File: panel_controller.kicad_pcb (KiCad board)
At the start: 2 copper layers, 105.5 x 88.5 mm, 17 parts, among them J1 Screw_Terminal_01x04, J2 SSW-104-01-F-S, J3 Screw_Terminal_01x03, J4 Screw_Terminal_01x02, J5 SSW-108-02-G-D, U1 ESP32-DEVKIT-V1

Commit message: pcb clock v1.5
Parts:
- moved H3 136.8 mm to (82.5, 125.0), turned to 180 degrees
- moved J5 105.8 mm to (121.4, 117.5), turned to -90 degrees
- moved H4 101.5 mm to (82.1, 48.0), turned to 0 degrees
- moved J4 94.9 mm to (95.5, 114.0), turned to -90 degrees
- moved J1 80.3 mm to (95.5, 53.5), turned to -90 degrees
- moved J3 77.7 mm to (95.5, 86.5), turned to -90 degrees
- moved H1 72.2 mm to (196.4, 47.9), turned to 0 degrees
- moved R7 71.5 mm to (109.4, 74.1), turned to 0 degrees
- moved R6 70.0 mm to (109.3, 67.5), turned to 0 degrees
- moved R5 69.6 mm to (109.3, 60.9), turned to 0 degrees
- moved H2 64.7 mm to (196.3, 124.8), turned to 180 degrees
- moved R1 55.4 mm to (124.5, 56.5), turned to 0 degrees
- moved R2 50.2 mm to (124.5, 63.1), turned to 0 degrees
- moved R3 46.2 mm to (124.5, 69.7), turned to 0 degrees
- moved R4 43.9 mm to (124.5, 76.2), turned to 0 degrees
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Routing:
- net Net-(U1-D23): track 141.6 -> 75.7 mm, vias 1 -> 0
- net +5V: track 55.8 -> 111.8 mm
- net Net-(U1-D15): track 103.8 -> 52.3 mm, vias 1 -> 2
- net Net-(U1-D4): track 99.7 -> 48.4 mm
- net Net-(U1-D19): track 121.0 -> 70.0 mm, vias 1 -> 2
- net Net-(U1-D2): track 97.2 -> 48.7 mm
- net Net-(U1-D5): track 105.8 -> 58.9 mm
- net Net-(U1-D18): track 116.1 -> 69.3 mm, vias 2 -> 1
- net Net-(U1-D32): track 30.7 -> 62.9 mm
- net Net-(U1-D33): track 28.7 -> 60.8 mm, vias 1 -> 0
- net Net-(J3-Pin_2): track 63.2 -> 95.0 mm, vias 0 -> 1
- net +3V3: track 116.3 -> 148.1 mm, vias 2 -> 1
- net Net-(U1-D22): track 58.1 -> 35.2 mm
- net Net-(J1-Pin_3): track 38.8 -> 18.3 mm
- net Net-(U1-D21): track 54.7 -> 34.3 mm
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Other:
- board size 105.5 x 88.5 mm -> 127.2 x 90 mm

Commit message: pcb clock v1.6
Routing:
- net Net-(U1-D14): track 87.1 -> 113.0 mm
- net +3V3: track 148.1 -> 167.4 mm, vias 1 -> 2
- net GND: track 200.6 -> 215.5 mm
- net Net-(U1-D26): track 92.2 -> 106.5 mm, vias 2 -> 0
- net +5V: track 111.8 -> 122.3 mm
- net Net-(U1-D18): track 69.3 -> 60.0 mm
- net Net-(U1-D25): track 78.0 -> 87.2 mm, vias 1 -> 2
- net Net-(J3-Pin_2): track 95.0 -> 102.1 mm, vias 1 -> 3
- net Net-(U1-D12): track 100.3 -> 95.7 mm, vias 2 -> 0
- net Net-(U1-D13): track 77.4 -> 81.5 mm, vias 1 -> 2
- net Net-(U1-D4): track 48.4 -> 52.5 mm
- net Net-(U1-D33): track 60.8 -> 57.7 mm
- net Net-(U1-D5): track 58.9 -> 55.9 mm
- net Net-(U1-D21): track 34.3 -> 37.2 mm, vias 0 -> 1
- net Net-(U1-D2): track 48.7 -> 46.1 mm
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
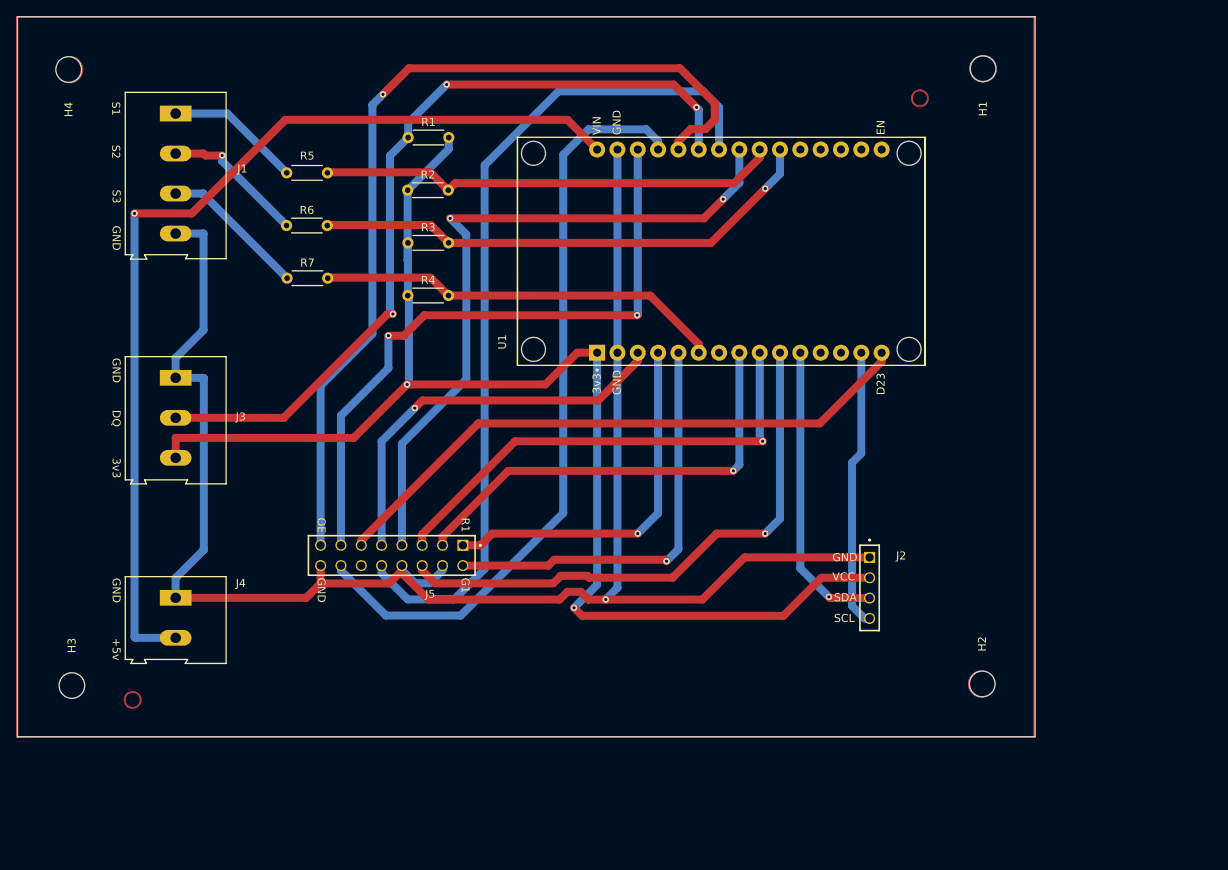
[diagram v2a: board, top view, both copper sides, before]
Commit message: pcb clock v1.7 rerouting for proper track width
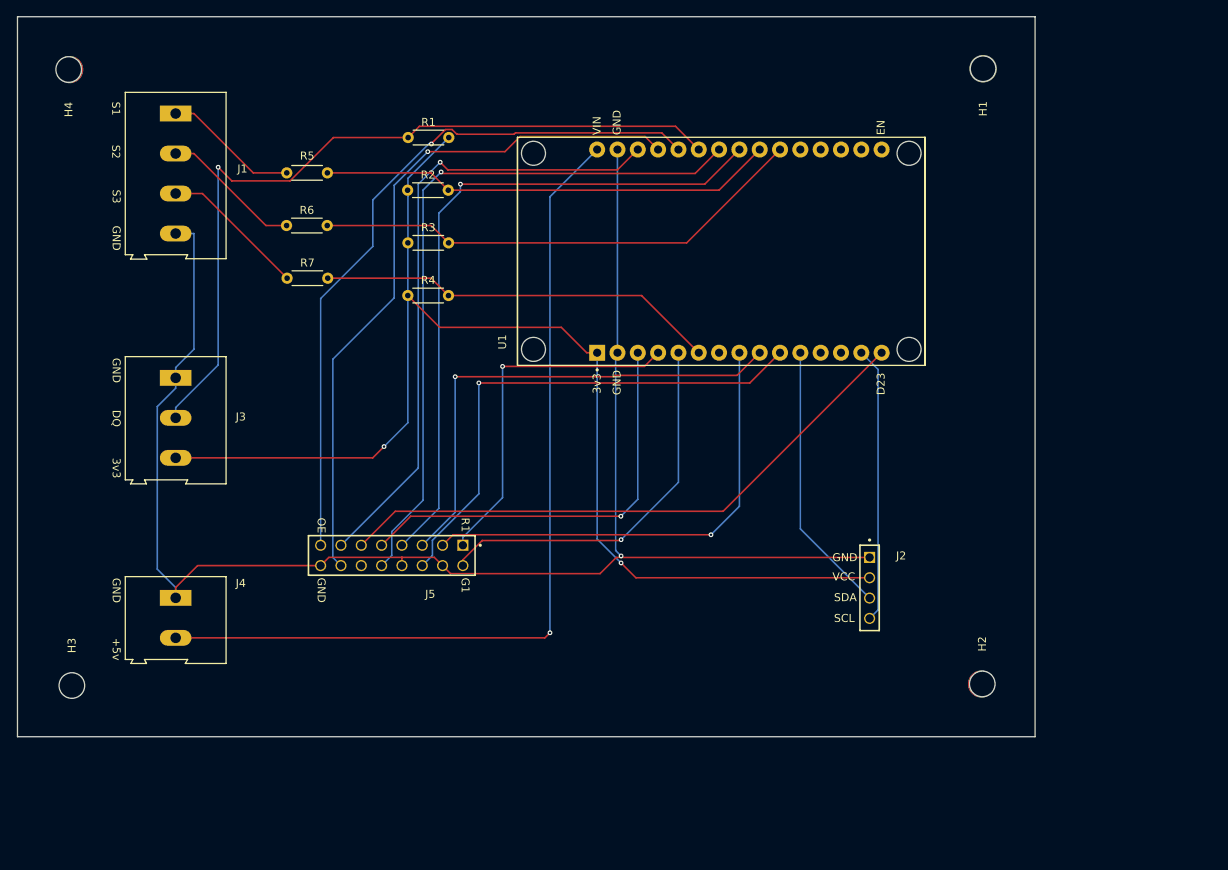
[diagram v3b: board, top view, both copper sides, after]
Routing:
- net Net-(U1-D14): track 113.0 -> 88.9 mm
- net GND: track 215.5 -> 194.3 mm
- net Net-(U1-D26): track 106.5 -> 88.3 mm, vias 0 -> 1
- net +5V: track 122.3 -> 109.9 mm
- net +3V3: track 167.4 -> 155.4 mm
- net Net-(U1-D12): track 95.7 -> 87.3 mm, vias 0 -> 1
- net Net-(U1-D19): track 70.3 -> 65.0 mm
- net Net-(U1-D4): track 52.5 -> 48.0 mm
- net Net-(J3-Pin_2): track 102.1 -> 98.3 mm, vias 3 -> 1
- net Net-(U1-D21): track 37.2 -> 34.3 mm, vias 1 -> 0
- net Net-(U1-D15): track 50.2 -> 52.7 mm
- net Net-(U1-D5): track 55.9 -> 58.3 mm
- net Net-(U1-D13): track 81.5 -> 79.2 mm, vias 2 -> 1
- net Net-(U1-D25): track 87.2 -> 84.8 mm, vias 2 -> 1
- net Net-(U1-D18): track 60.0 -> 62.1 mm
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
